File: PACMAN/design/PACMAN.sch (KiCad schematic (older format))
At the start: 27 parts, among them IC1 ATTINY85-P, IC2 74VHC4052_ANALOG_MUX, U1 LM7805, U2 ARDUINO_PRO_MINI

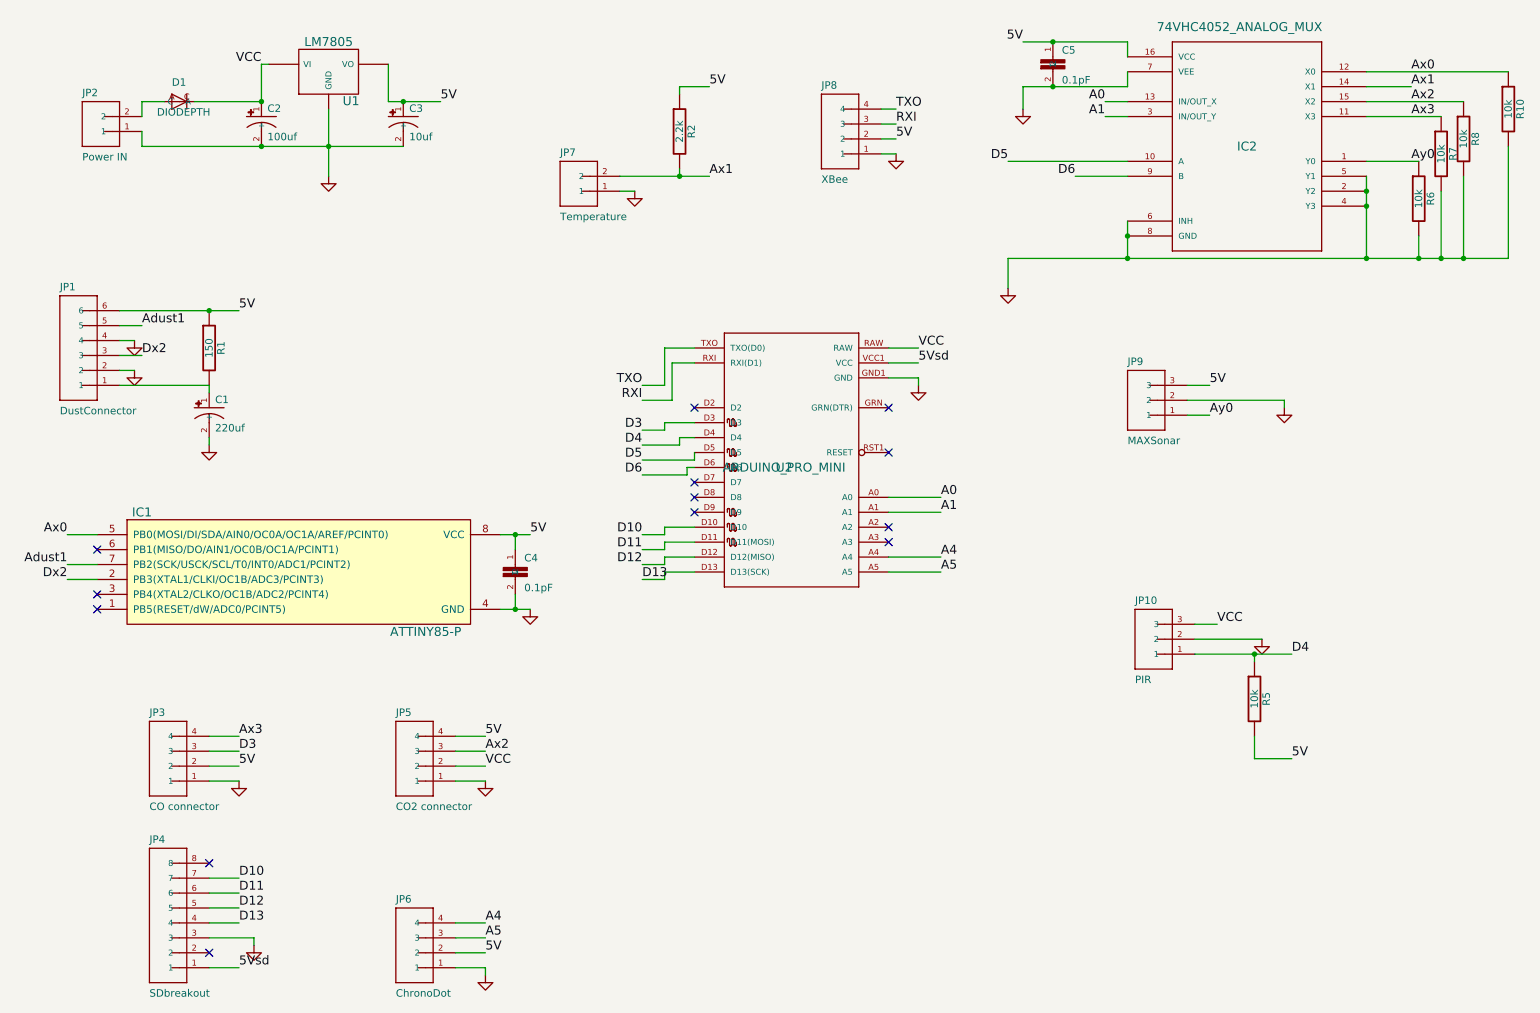
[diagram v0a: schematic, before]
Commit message: New Home page. Updated PACMAN firmware. Updated data parsing.
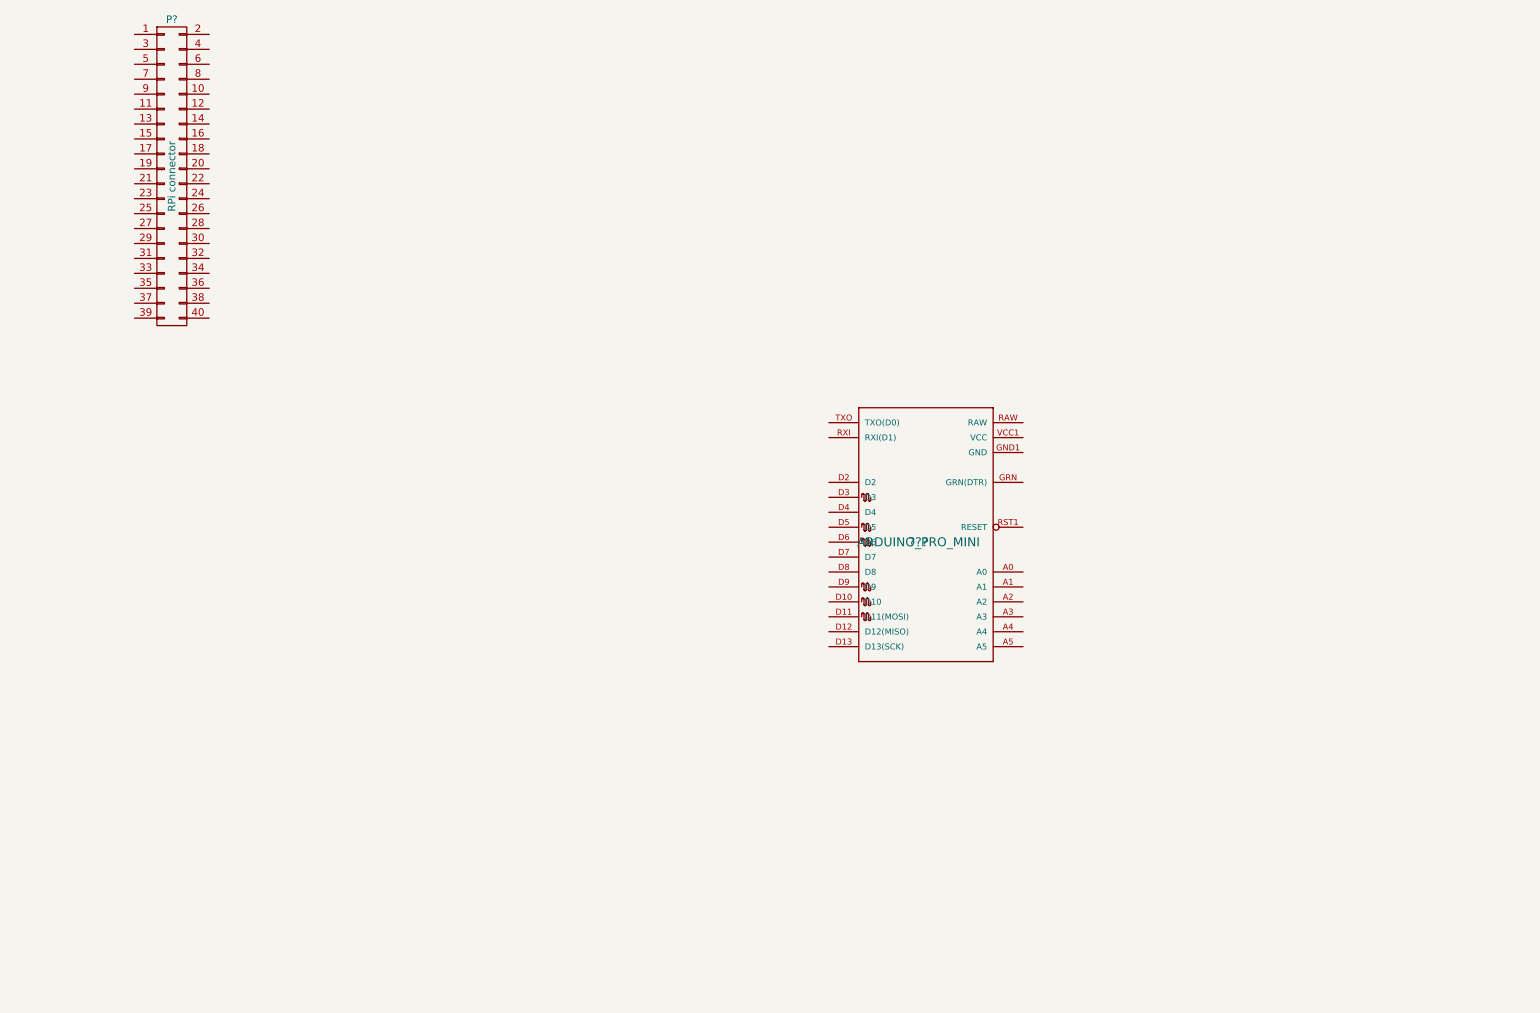
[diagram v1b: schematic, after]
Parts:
- removed C1: 220uf, SparkFun-CPOL-RADIAL-100UF-25V, symbol CAP_POLPTH1
- removed C2: 100uf, SparkFun-CPOL-RADIAL-10UF-25V, symbol CAP_POLPTH2
- removed C3: 10uf, SparkFun-CPOL-RADIAL-10UF-25V, symbol CAP_POLPTH2
- removed C4, C5: 0.1pF, SparkFun-CAP-PTH-SMALL, symbol CAPPTH
- removed D1: DIODEPTH, SparkFun-DIODE-1N4001, symbol DIODEPTH
- removed IC1: ATTINY85-P, DIP8, symbol ATTINY85-P
- removed IC2: 74VHC4052_ANALOG_MUX, symbol 74VHC4052_ANALOG_MUX
- removed JP1: DustConnector, SparkFun-1X06_LOCK, symbol M06LOCK
- removed JP10: PIR, SparkFun-1X03_LONGPADS, symbol M03LONGPADS
- removed JP2: Power IN, SparkFun-1X02, symbol M02PTH
- removed JP3: CO connector, SparkFun-1X04, symbol M04PTH
- removed JP4: SDbreakout, SparkFun-1X08_LOCK, symbol M08LOCK
- removed JP5: CO2 connector, SparkFun-1X04, symbol M04PTH
- removed JP6: ChronoDot, SparkFun-1X04, symbol M04PTH
- removed JP7: Temperature, SparkFun-1X02, symbol M02PTH
- removed JP8: XBee, SparkFun-1X04, symbol M04PTH
- removed JP9: MAXSonar, SparkFun-1X03_LONGPADS, symbol M03LONGPADS
- removed R1: 150, symbol R
- removed R10, R5, R6, R7, R8: 10k, symbol R
- removed R2: 2.2k, symbol R
- removed U1: LM7805, symbol LM7805
- removed U2: ARDUINO_PRO_MINI, symbol ARDUINO_PRO_MINI
- added ???: ARDUINO_PRO_MINI, symbol ARDUINO_PRO_MINI
- added P?: RPi connector, symbol CONN_02X20
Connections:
- no-connect marks 13 -> 0

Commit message: Raspberry Pi B+ hat for Dusty-ACorn ready for manufacture
Signed-off-by: Gustavo Olivares <guolivar@gmail.com>
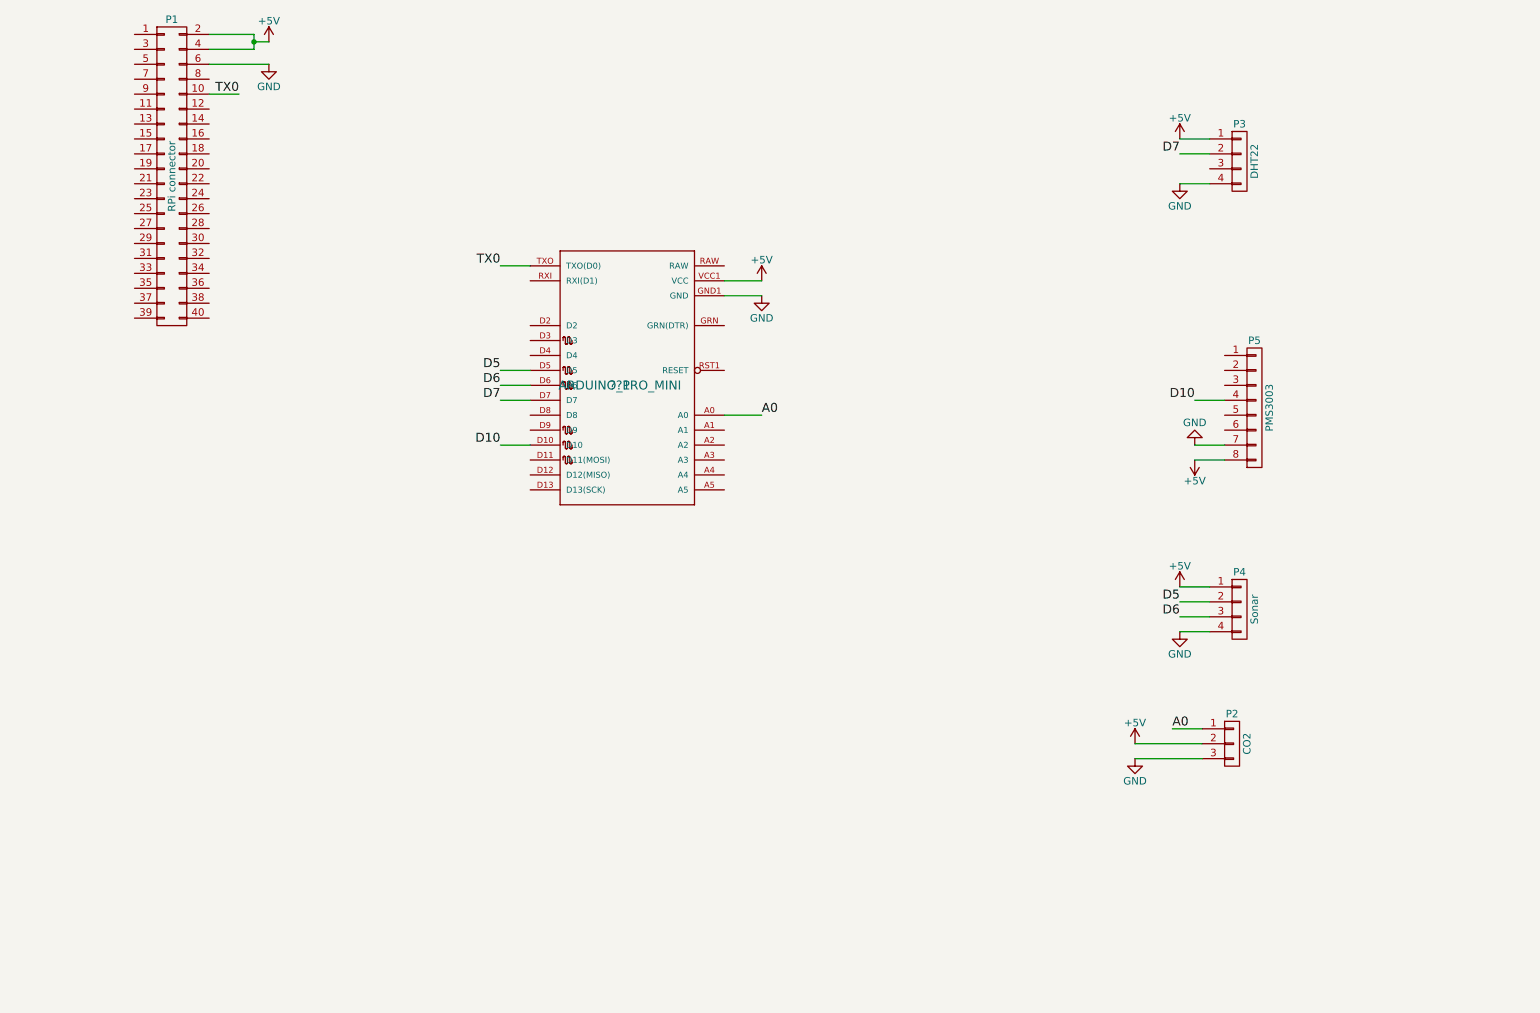
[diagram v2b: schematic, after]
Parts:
- added P2: CO2, Pin_Headers:Pin_Header_Straight_1x03, symbol CONN_01X03
- added P3: DHT22, Pin_Headers:Pin_Header_Straight_1x04, symbol CONN_01X04
- added P4: Sonar, Pin_Headers:Pin_Header_Straight_1x04, symbol CONN_01X04
- added P5: PMS3003, Connectors_Molex:Connector_Molex_PicoBlade_53261-0871, symbol CONN_01X08
- ??1: renamed from ???; footprint (none) -> arduino_pro_mini_V2:Halley-ARDUINO_PRO_MINI
- P1: renamed from P?; footprint (none) -> headers:Pin_Header_Straight_2x20_SMD
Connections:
- net A0: now reaches ??1.A0
- net A0: now also P2.1 (P1)
- net D10: now reaches ??1.D10
- net D10: now also P5.4 (P4)
- net D5: now reaches ??1.D5
- net D5: now also P4.2 (P2)
- net D6: now reaches ??1.D6
- net D6: now also P4.3 (P3)
- net D7: now reaches ??1.D7
- net D7: now also P3.2 (P2)
- net GND: now reaches ??1.GND1 (GND)
- net GND: now also P1.6 (P6), P2.3 (P3), P3.4 (P4), P4.4 (P4), P5.7 (P7)
- net TX0: now reaches ??1.TXO (TXO(D0))
- net TX0: now also P1.10 (P10)
- net +5V: now reaches ??1.VCC1 (VCC)
- net +5V: now also P1.2 (P2), P1.4 (P4), P2.2 (P2), P3.1 (P1), P4.1 (P1), P5.8 (P8)
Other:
- moved on the sheet: ??1

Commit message: Merging work at work to prepare deployment
Signed-off-by: Gustavo Olivares <guolivar@gmail.com>
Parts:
- MC1: renamed from ??1; footprint arduino_pro_mini_V2:Halley-ARDUINO_PRO_MINI -> arduino:Halley-ARDUINO_PRO_MINI
- P1: footprint headers:Pin_Header_Straight_2x20_SMD -> Pin_Headers:Pin_Header_Straight_2x20
- P5: footprint Connectors_Molex:Connector_Molex_PicoBlade_53261-0871 -> Pin_Headers:Pin_Header_Straight_1x08
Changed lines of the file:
@@
 LIBS:valves
 LIBS:gus_work
-LIBS:Halley
-LIBS:adafruit
 LIBS:PACMAN-cache
 EELAYER 25 0
@@
 $EndDescr
 $Comp
-L ARDUINO_PRO_MINI ??1
+L ARDUINO_PRO_MINI MC1
 U 1 1 57731415
 P 4700 3300
-F 0 "??1" H 4700 3300 60  0000 C CNN
+F 0 "MC1" H 4700 3300 60  0000 C CNN
 F 1 "ARDUINO_PRO_MINI" H 4700 3300 60  0000 C CNN
-F 2 "arduino_pro_mini_V2:Halley-ARDUINO_PRO_MINI" H 4700 3300 60  0001 C CNN
+F 2 "arduino:Halley-ARDUINO_PRO_MINI" H 4700 3300 60  0001 C CNN
 F 3 "" H 4700 3300 60  0000 C CNN
 	1    4700 3300
@@
 F 0 "P1" H 1700 2950 50  0000 C CNN
 F 1 "RPi connector" V 1700 1900 50  0000 C CNN
-F 2 "headers:Pin_Header_Straight_2x20_SMD" H 1700 950 50  0001 C CNN
+F 2 "Pin_Headers:Pin_Header_Straight_2x20" H 1700 950 50  0001 C CNN
 F 3 "" H 1700 950 50  0000 C CNN
 	1    1700 1900
@@
 F 0 "P5" H 8950 3900 50  0000 C CNN
 F 1 "PMS3003" V 9050 3450 50  0000 C CNN
-F 2 "Connectors_Molex:Connector_Molex_PicoBlade_53261-0871" H 8950 3450 50  0001 C CNN
+F 2 "Pin_Headers:Pin_Header_Straight_1x08" H 8950 3450 50  0001 C CNN
 F 3 "" H 8950 3450 50  0000 C CNN
 	1    8950 3450
